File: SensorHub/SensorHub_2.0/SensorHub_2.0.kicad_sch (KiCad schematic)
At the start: 43 parts, among them J2 Conn_01x03, J3 Conn_01x05, J4 USB_C_Receptacle, U1 R7FA4E2B93CFM#AA0, U2 MYRGM080200C41RA, U3 TJA1051TK-3, U4 BMI270, U5 ASCODV-24.000MHZ-LR-T3

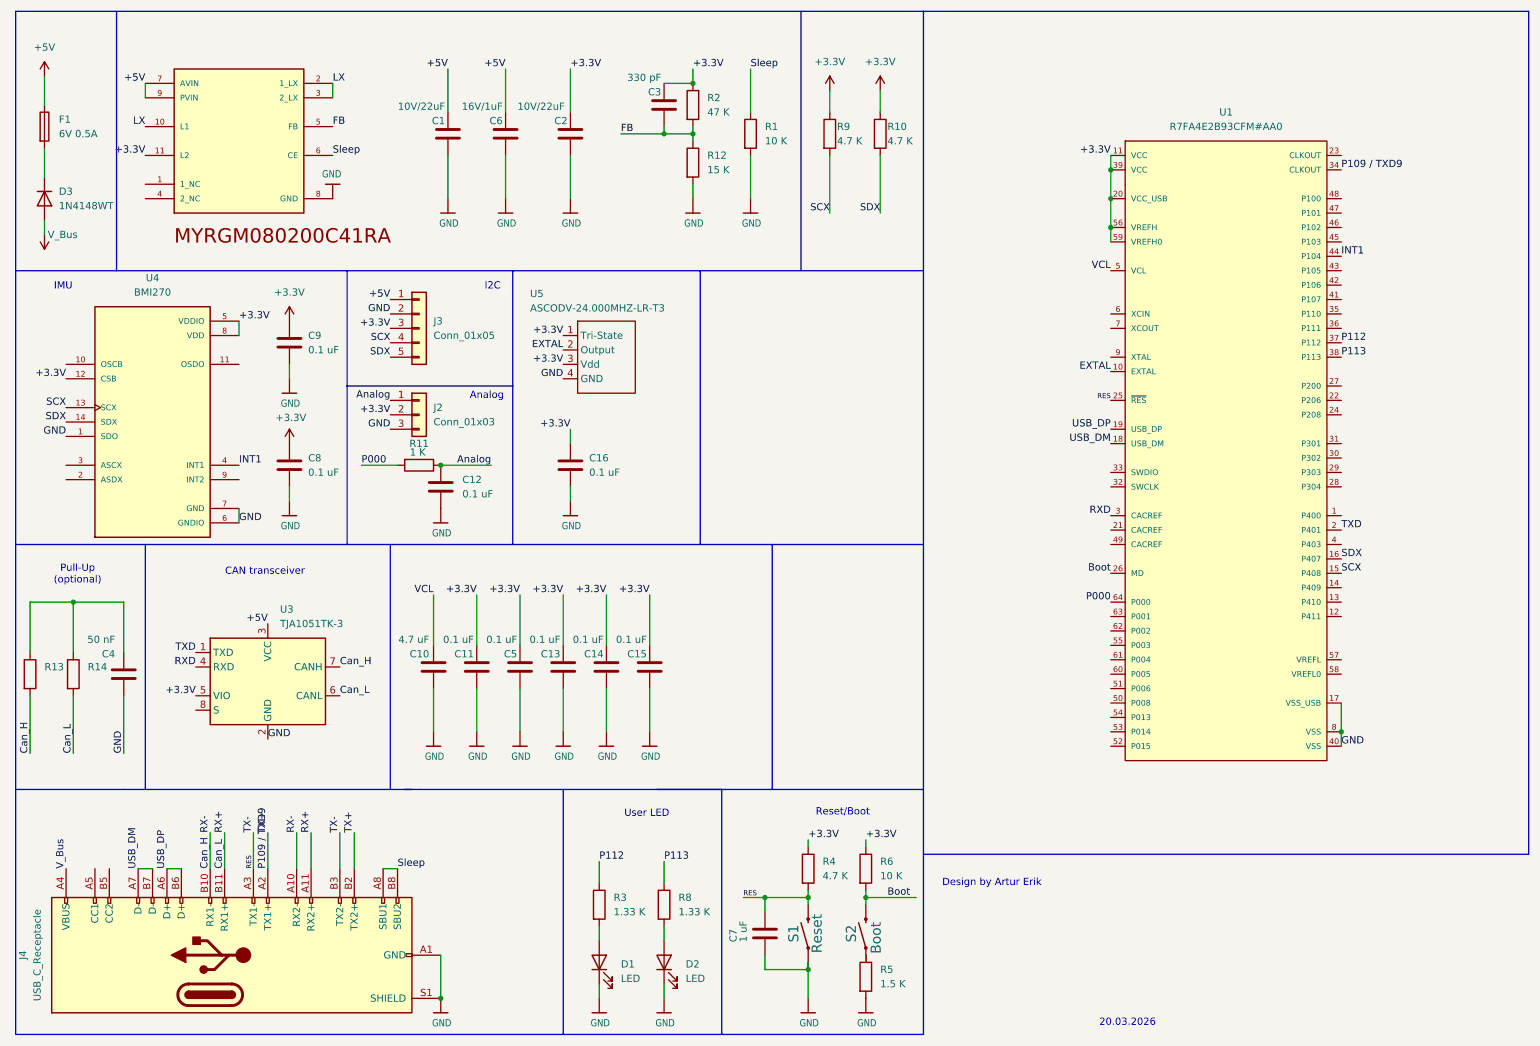
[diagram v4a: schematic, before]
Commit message: New connector BM46B-12DP-0.35V(53)
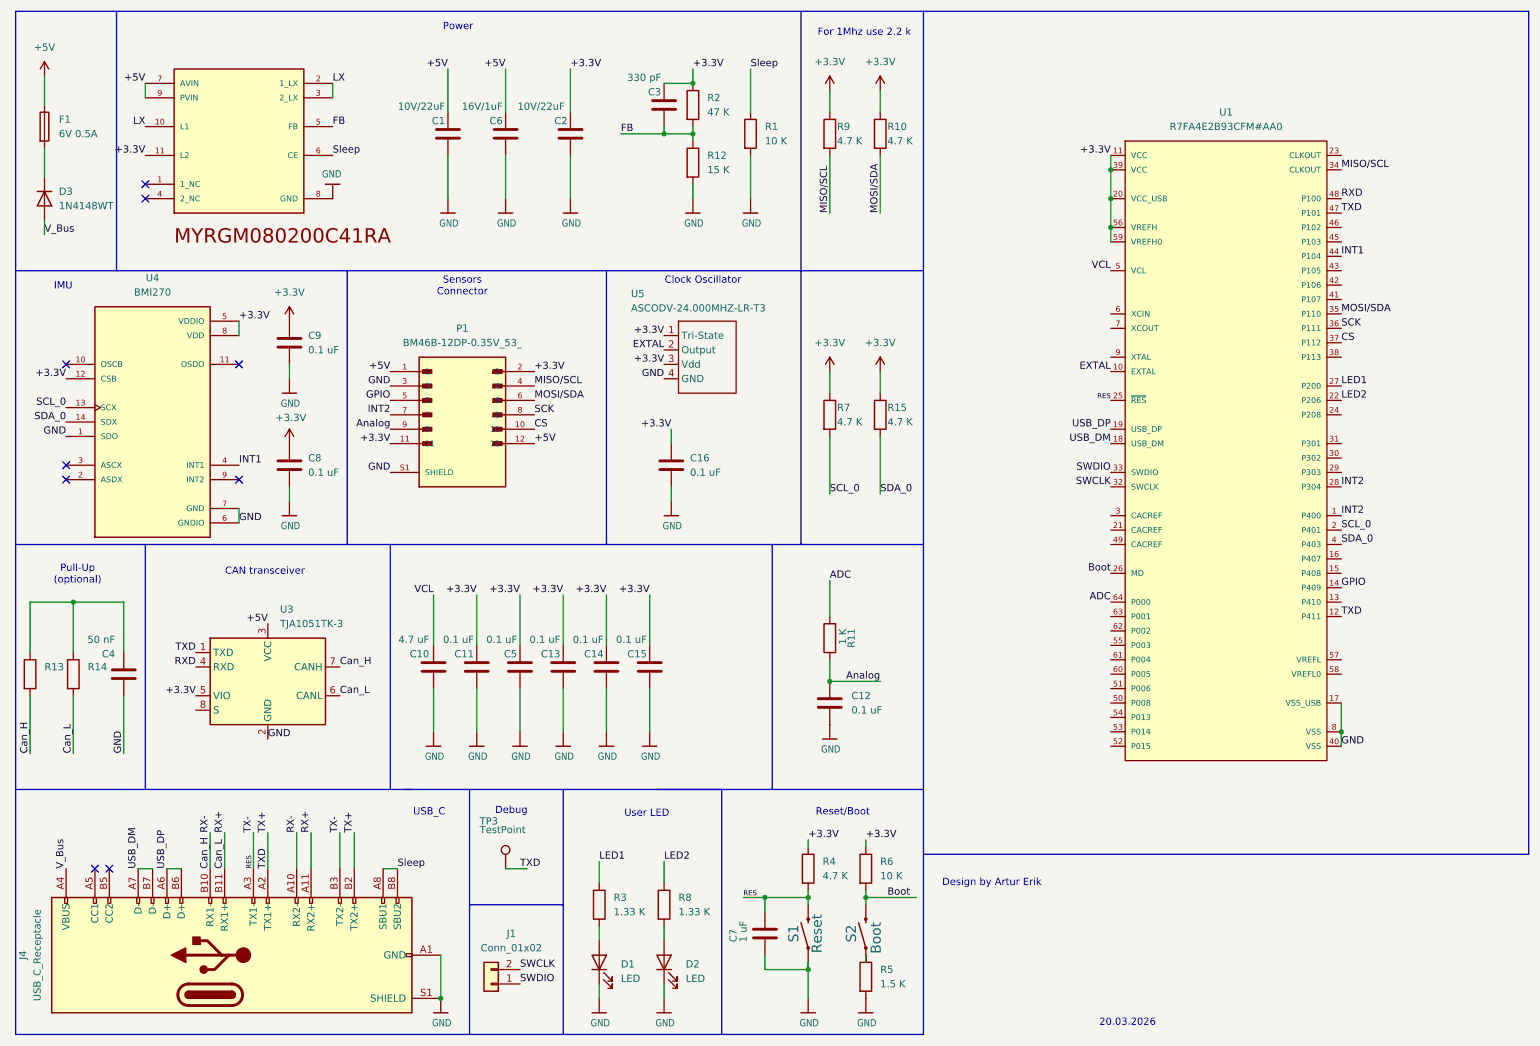
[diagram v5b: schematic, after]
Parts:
- removed J2: Conn_01x03, Connector_PinHeader_2.54mm:PinHeader_1x03_P2.54mm_Vertical, symbol Connector_Generic:Conn_01x03
- removed J3: Conn_01x05, Connector_PinHeader_2.54mm:PinHeader_1x05_P2.54mm_Vertical, symbol Connector_Generic:Conn_01x05
- added J1: Conn_01x02, Connector_PinSocket_1.00mm:PinSocket_1x02_P1.00mm_Vertical, symbol Connector_Generic:Conn_01x02
- added P1: BM46B-12DP-0.35V_53_, BM46B-12DP-0.35V_53_:HRS_BM46B-12DP-0.35V_53_, symbol BM46B-12DP-0.35V_53_:BM46B-12DP-0.35V_53_
- added R15, R7: 4.7 K, Resistor_SMD:R_0201_0603Metric, symbol Device:R
- added TP3: TestPoint, TestPoint:TestPoint_THTPad_D1.0mm_Drill0.5mm, symbol Connector:TestPoint
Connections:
- net +3.3V: now also P1.11, P1.2, R15.1, R7.1
- net +5V: now also P1.1, P1.12
- net Analog: now also P1.9
- net GND: now also P1.3, P1.S1 (SHIELD), P1.S2 (SHIELD), P1.S3 (SHIELD), P1.S4 (SHIELD)
- net RXD: now also U1.48 (P100); no longer U1.3 (CACREF)
- net INT2: now reaches U1.1 (P400)
- net INT2: now also U1.28 (P304), P1.7
- net TX+: now reaches U1.12 (P411)
- net TX+: now also J4.A2 (TX1+), J4.B2 (TX2+), U1.47 (P101), U3.1 (TXD), TP3.1
- net GPIO: now reaches U1.14 (P409)
- net GPIO: now also P1.5
- net LED2: now reaches U1.22 (P206)
- net LED2: now also R8.1
- net LED1: now reaches U1.27 (P200)
- net LED1: now also R3.1
- net SWCLK: now reaches U1.32 (SWCLK)
- net SWCLK: now also J1.2 (Pin_2)
- net SWDIO: now reaches U1.33 (SWDIO)
- net SWDIO: now also J1.1 (Pin_1)
- net MOSI/SDA: now reaches U1.35 (P110)
- net MOSI/SDA: now also R10.2, P1.6
- net SCK: now reaches U1.36 (P111)
- net SCK: now also P1.8
- net SDA_0: now reaches U1.4 (P403)
- net SDA_0: now also U4.14 (SDX), R15.2
- net P000 renamed ADC
- removed net P109 / TXD9: J4.A2 (TX1+), J4.B2 (TX2+), U1.34 (CLKOUT)
- net P112 renamed CS
- net CS: now also P1.10; no longer R3.1
- net P113: no longer names the net of U1.38 (P113)
- net P113: no longer R8.1
- removed net SCX: R9.2, U1.15 (P408), U4.13 (SCX)
- removed net SDX: R10.2, U1.16 (P407), U4.14 (SDX)
- net TXD renamed SCL_0
- net SCL_0: now also U4.13 (SCX), R7.2; no longer U3.1 (TXD)
- new net MISO/SCL: P1.4, R9.2, U1.34 (CLKOUT)
- no-connect marks 0 -> 9
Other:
- note added: "Clock Oscillator"
- note added: "Debug"
- note added: "For 1Mhz use 2.2 k"
- note added: "Power"
- note added: "Sensors Connector"
- note added: "USB_C"
- note removed: "Analog"
- note removed: "I2C"
- moved on the sheet: C12, C16, R11, U5

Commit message: New testPoints and Res filter
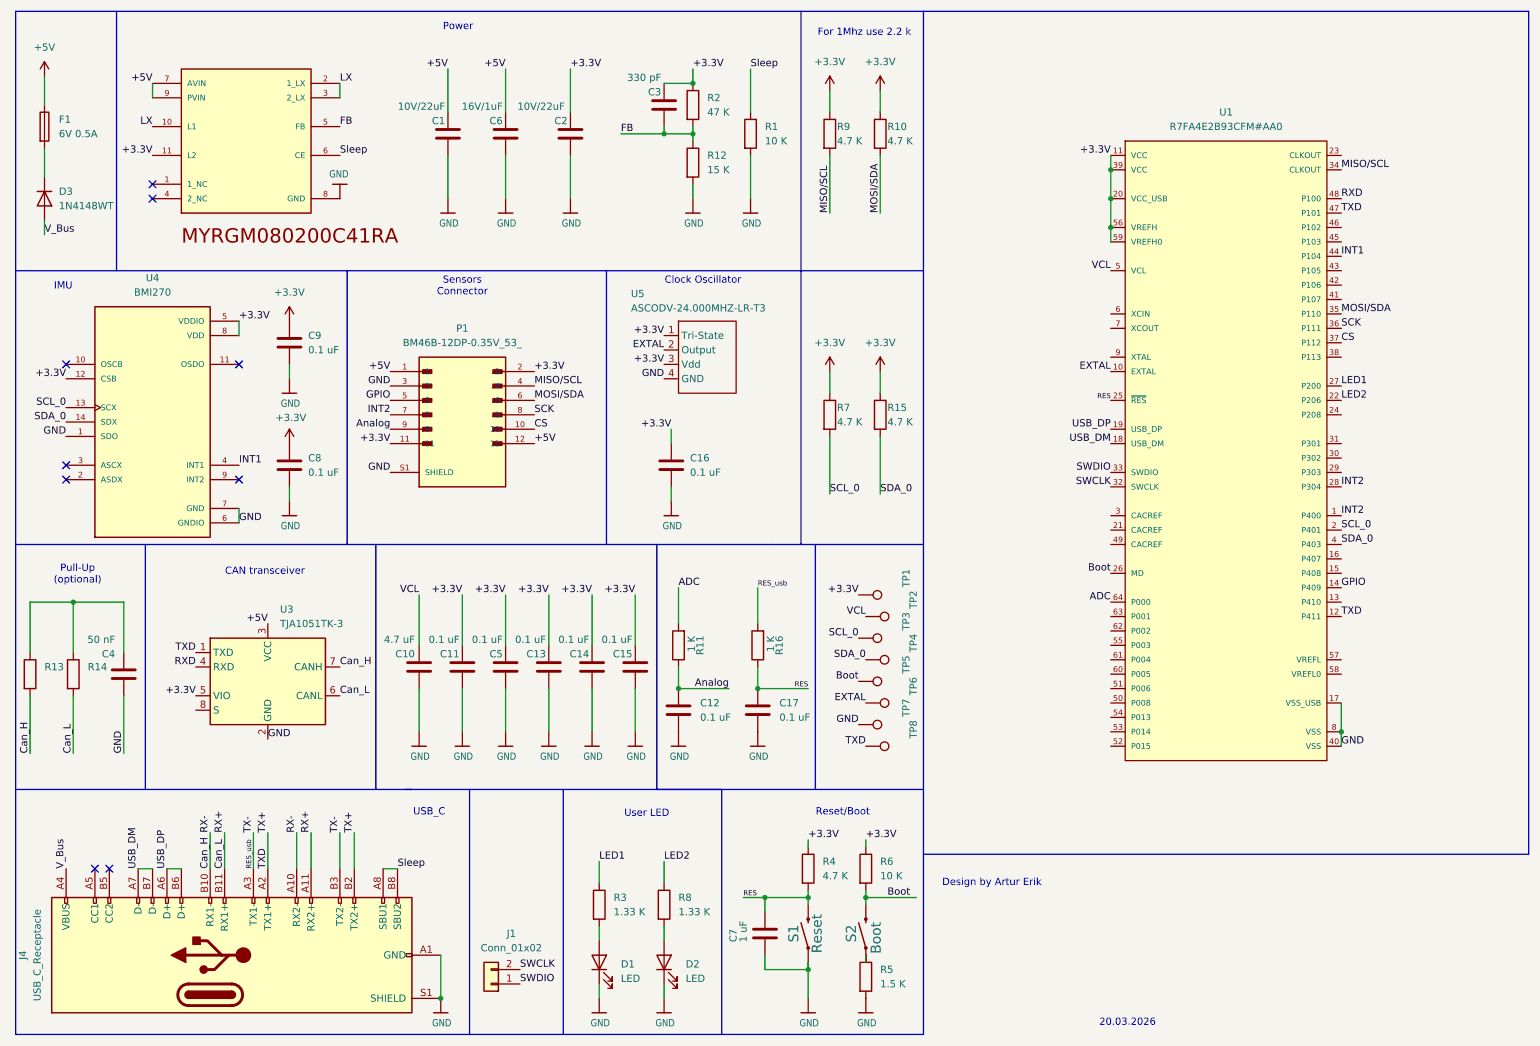
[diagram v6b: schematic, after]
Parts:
- added C17: 0.1 uF, Capacitor_SMD:C_0603_1608Metric, symbol Device:C
- added R16: 1 K, Resistor_SMD:R_0201_0603Metric, symbol Device:R
- added TP1, TP2, TP4, TP5, TP6, TP7, TP8: TestPoint, TestPoint:TestPoint_THTPad_D1.0mm_Drill0.5mm, symbol Connector:TestPoint
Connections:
- net +3.3V: now also TP1.1
- net Boot: now also TP5.1
- net EXTAL: now also TP6.1
- net GND: now also C17.2, TP7.1
- net RES: now also C17.1, R16.1; no longer J4.A3 (TX1-), J4.B3 (TX2-)
- net SCL_0: now also TP3.1
- net SDA_0: now also TP4.1
- net TX+: now also TP8.1; no longer TP3.1
- net VCL: now also TP2.1
- new net RES_usb: J4.A3 (TX1-), J4.B3 (TX2-), R16.2
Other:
- note removed: "Debug"
- moved on the sheet: C10, C11, C12, C13, C14, C15, C5, R11, TP3

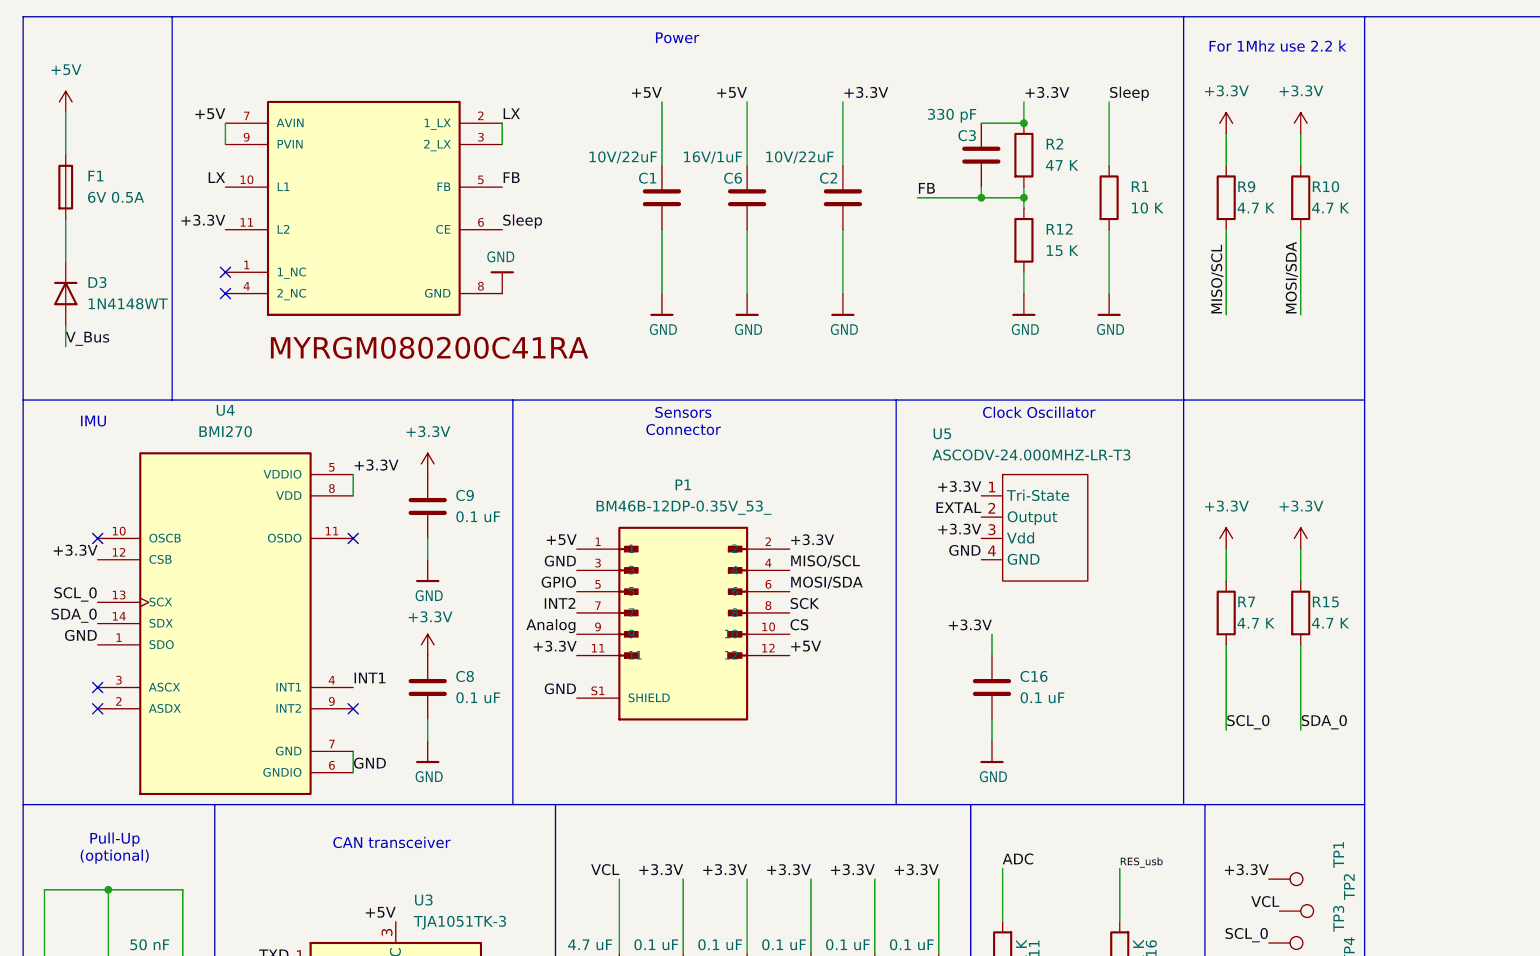
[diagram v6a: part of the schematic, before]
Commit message: Mirrored connector
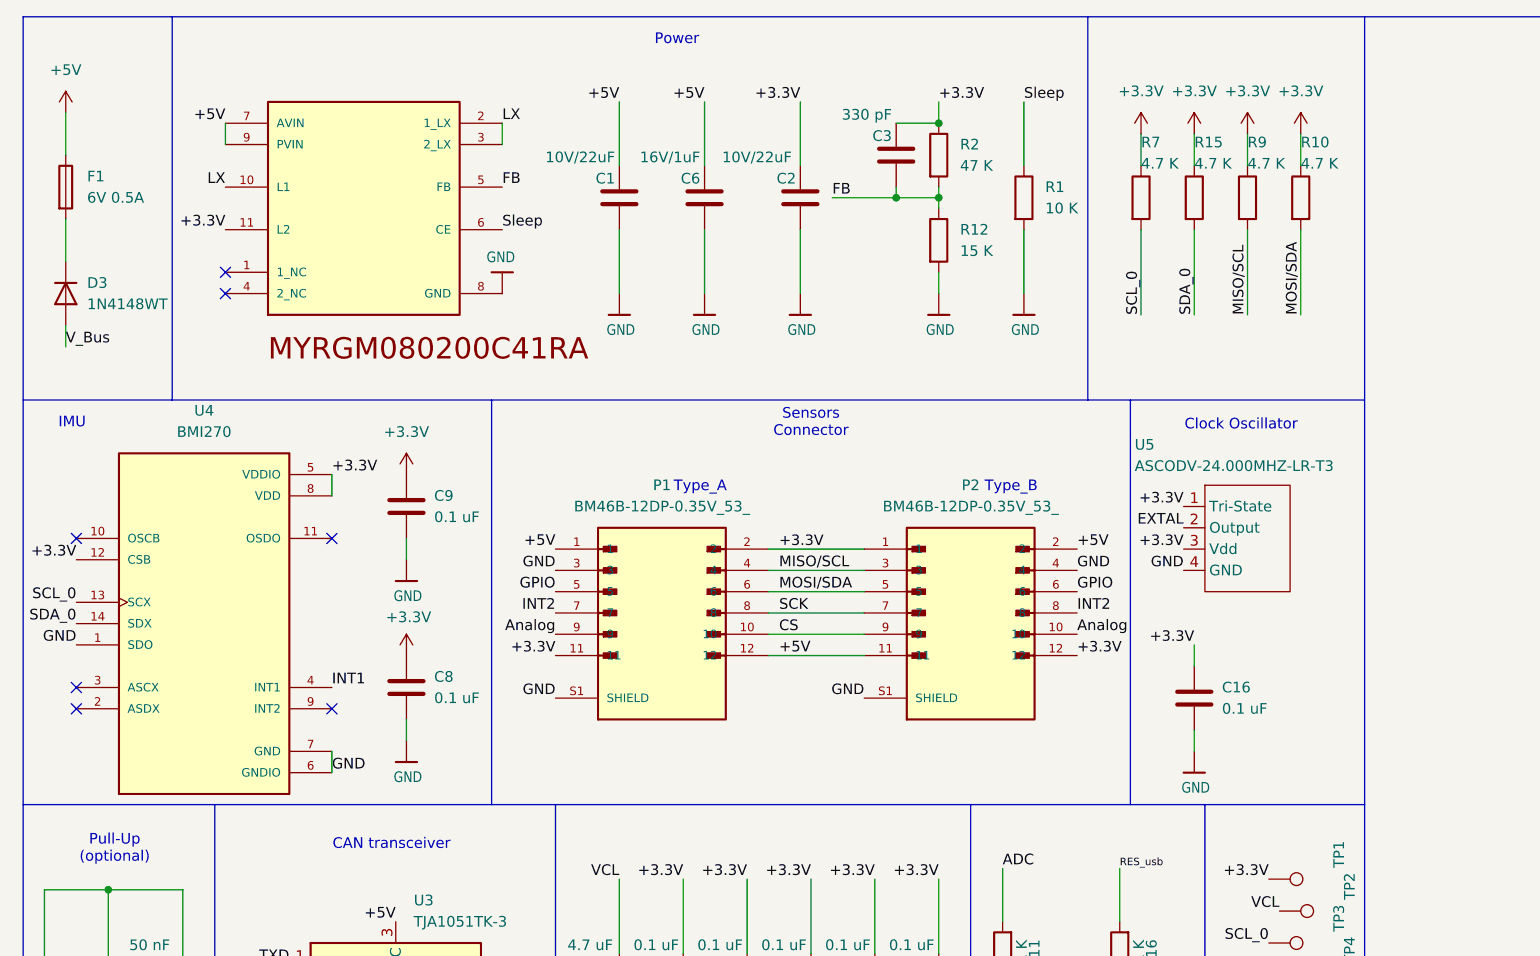
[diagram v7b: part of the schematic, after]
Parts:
- added P2: BM46B-12DP-0.35V_53_, BM46B-12DP-0.35V_53_:HRS_BM46B-12DP-0.35V_53_, symbol BM46B-12DP-0.35V_53_:BM46B-12DP-0.35V_53_
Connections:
- net +3.3V: now also P2.1, P2.12
- net +5V: now also P2.11, P2.2
- net Analog: now also P2.10
- net CS: now also P2.9
- net GND: now also P2.4, P2.S1 (SHIELD), P2.S2 (SHIELD), P2.S3 (SHIELD), P2.S4 (SHIELD)
- net GPIO: now also P2.6
- net INT2: now also P2.8
- net MISO/SCL: now also P2.3
- net MOSI/SDA: now also P2.5
- net SCK: now also P2.7
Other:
- note added: "Type_A"
- note added: "Type_B"
- note removed: "For 1Mhz use 2.2 k"
- moved on the sheet: C1, C16, C2, C3, C6, C8, C9, P1, R1, R12, R2, U4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
